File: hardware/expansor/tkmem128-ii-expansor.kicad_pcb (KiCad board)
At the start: 2 copper layers, 78.7 x 45 mm, 3 parts, among them J1 Terminais do conector, J2 Passagem

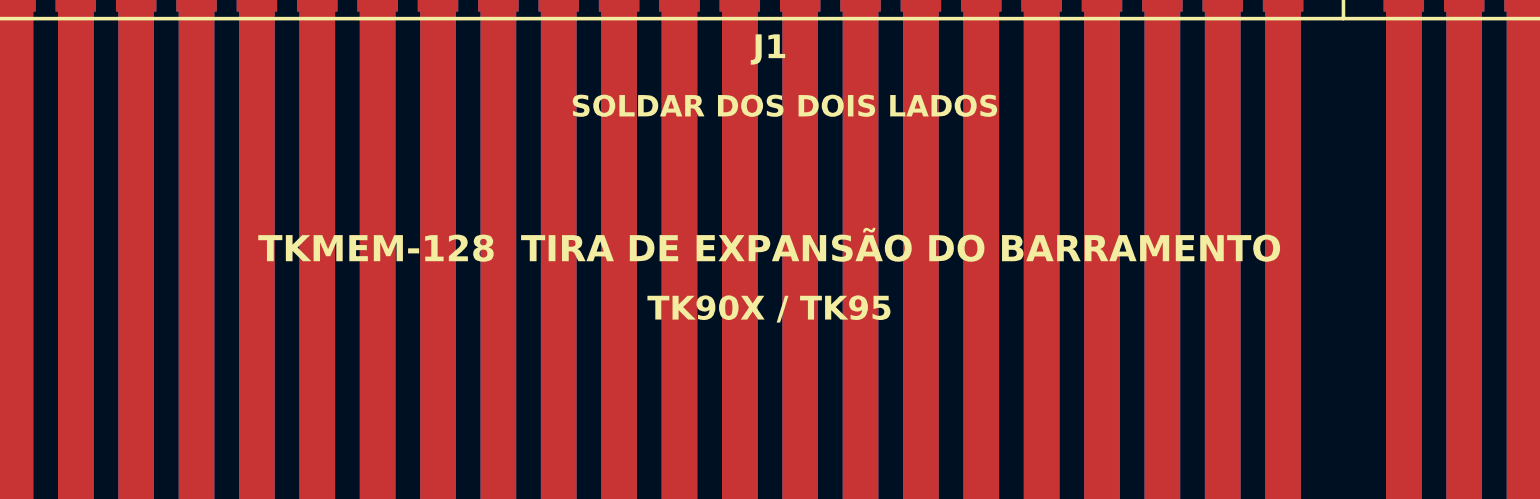
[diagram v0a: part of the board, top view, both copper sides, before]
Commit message: Projeto passa a se chamar TKMEM-128 II
"TKMEM-128 KiCad" dizia so que mudou de software de CAD, quando na verdade a
placa e outra: 4 camadas, trilha do dobro, roteamento e posicionamento refeitos,
JP4 e SJ1/SJ2 fora, auto-desativacao em outro pino, compatibilidade com o ZX
Spectrum recuperada. "II" nomeia a geracao, e manter "TKMEM-128" no nome mantem
a linhagem visivel.

O CUIDADO PRINCIPAL foi nao apagar o credito. "TKMEM-128" aparece no repositorio
nos dois sentidos, e so o primeiro virou "II":

  a NOSSA placa  titulo do README, serigrafia das duas placas, gal/README, duas
                 frases do PREPARAR-O-TK
  a do LUCCAS    a linha da tabela de derivacao, o diagrama de linhagem, "o autor
                 da TKMEM-128 original deixou de fornecer a ROM", e o titulo do
                 artigo dele citado no PREPARAR-O-TK — esses ficaram intactos

Uma substituicao global teria reescrito a atribuicao, que e justamente o que a
CERN-OHL-S existe para proteger.

ARQUIVOS. Os do projeto KiCad seguiram o nome:

  hardware/tkmem128.kicad_{pro,sch,pcb,dru}          -> tkmem128-ii.*
  hardware/expansor/tkmem128-expansor.*             -> tkmem128-ii-expansor.*
  gerbers                                            -> tkmem128-ii-F_Cu.gbr etc.

A BIBLIOTECA NAO. `hardware/lib/tkmem128.pretty` e `tkmem128.kicad_sym` continuam
com o nome antigo de proposito: sao um acervo de footprints do barramento do TK,
nao do projeto, e renomea-las obrigaria a reescrever o prefixo `tkmem128:` em
cada componente das duas placas — superficie de erro sem ganho. Mesmo raciocinio
para `hardware/gal/tkmem128.pld/.jed`, que e o mapa de fusiveis herdado.

Repositorio renomeado para github.com/lrrosa/tkmem128-ii (o GitHub redireciona o
endereco antigo). A URL na serigrafia das duas placas acompanhou.

De quebra: com tres caracteres a mais, o titulo na serigrafia da principal — que
e centralizado — cresceu para os dois lados e encostou em R4. Deslocado 5 mm.

DRC 0/0 na principal, 0 violacoes na t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
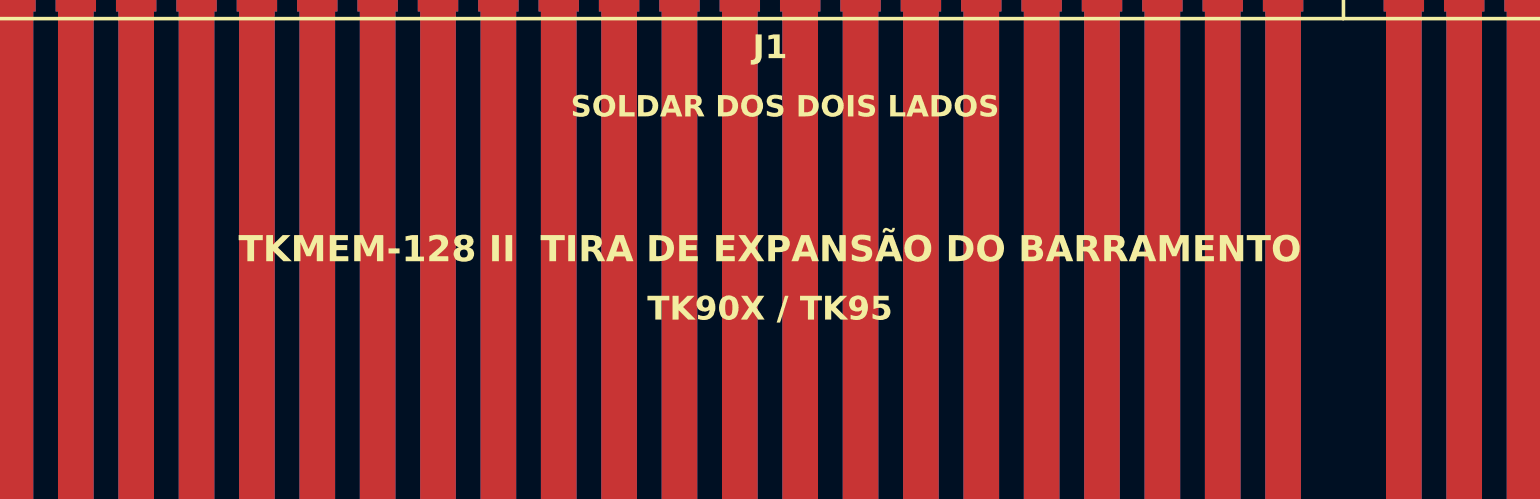
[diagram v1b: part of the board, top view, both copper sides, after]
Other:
- board text added: "CERN-OHL-S v2 | github.com/lrrosa/tkmem128-ii"
- board text added: "TKMEM-128 II TIRA DE EXPANSÃO DO BARRAMENTO"
- board text removed: "CERN-OHL-S v2 | github.com/lrrosa/tkmem128-kicad"
- board text removed: "TKMEM-128 TIRA DE EXPANSÃO DO BARRAMENTO"
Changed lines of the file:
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@@
 		)
 	)
-	(gr_text "TKMEM-128  TIRA DE EXPANSÃO DO BARRAMENTO"
+	(gr_text "TKMEM-128 II  TIRA DE EXPANSÃO DO BARRAMENTO"
 		(at 39.37 15 0)
 		(layer "F.SilkS")
@@
 		)
 	)
-	(gr_text "CERN-OHL-S v2  |  github.com/lrrosa/tkmem128-kicad"
+	(gr_text "CERN-OHL-S v2  |  github.com/lrrosa/tkmem128-ii"
 		(at 39.37 22 0)
 		(layer "B.SilkS")

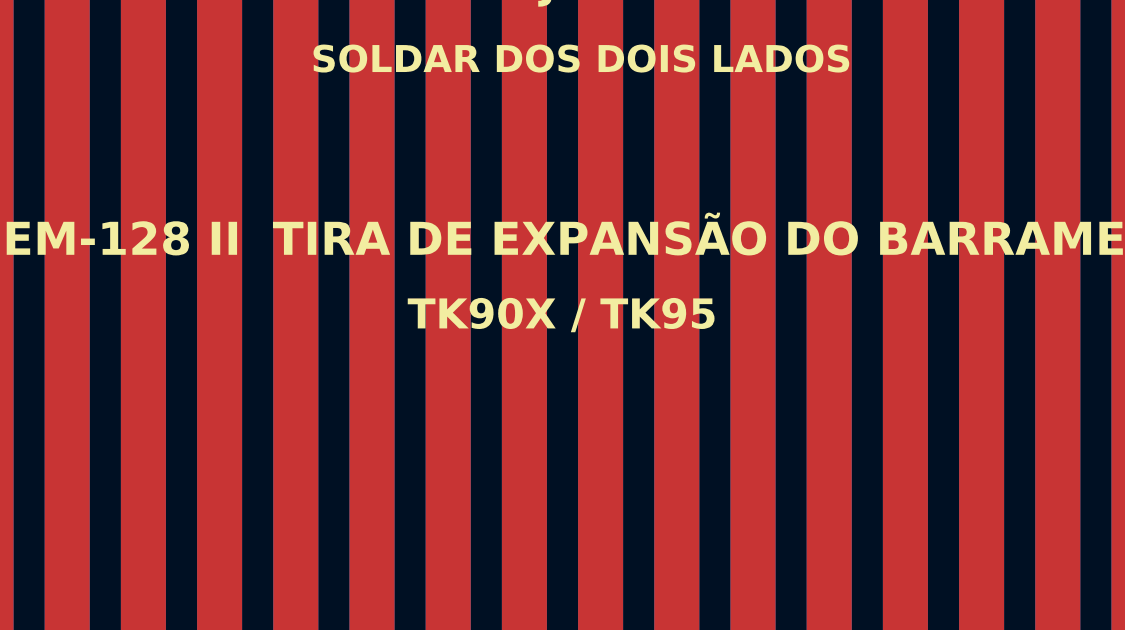
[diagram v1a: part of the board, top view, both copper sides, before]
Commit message: Legenda diz ZX Spectrum 48K e clones — e o pino 17 parou de mentir
O bloco de titulo dos dois esquematicos dizia "para TK90X/TK95". Errado desde
que a placa voltou a servir no ZX Spectrum 48K: o circuito e do Velesoft e
nasceu para o Spectrum, os TKs e que sao os clones. Agora diz "ZX Spectrum 48K
e clones", e o mesmo vale para o titulo em netlist.py/netlist_exp.py e para as
descricoes de simbolo e footprint.

De quebra, a mesma afirmacao errada estava na SERIGRAFIA da tira, em F.SilkS —
essa sai impressa na placa. Virou "ZX SPECTRUM 48K E CLONES".

Os `tags`/`ki_keywords` continuam citando TK90X e TK95 de proposito: ali listar
as duas familias e justamente o que se quer, sao palavras de busca.

O QUE APARECEU AO REGERAR A BIBLIOTECA. O simbolo do conector ainda rotulava
**pino 17 = RAMDIS e pino 29 = NC** — a pinagem de ANTES de mover a
auto-desativacao da RAM para o pino 29 por causa do video componente do
Spectrum. E tinha chegado aos dois esquematicos: o PDF entregue desenhava
exatamente a ligacao que fomos evitar, com o rotulo do pino contradizendo o
fio ligado nele (o global label ja dizia BUS_P17). Quatro rotulos por
esquematico: 16, 17, 18 e 29.

E a terceira vez que uma copia envelhece em silencio aqui — antes foram a ilha
do conector (biblioteca com 1,75 enquanto a placa usava 1,50) e o titulo do
bloco de legenda. Entao virou conferidor: `tools/confere_pinos.py` compara os
rotulos dos dois esquematicos e da biblioteca contra busdef.py, que e a fonte
unica da pinagem. Conferido com teste negativo nos dois formatos.

Detalhe que quase deixou o conferidor inutil: o gerador escreve "ROTULO (nn)"
com espaco, e e assim que fica no .kicad_sym, mas o KiCad troca por underscore
ao salvar um .kicad_sch. A primeira versao do padrao so aceitava underscore,
lia ZERO pino na biblioteca e passava "sem divergencia".

DRC 0/0 na principal, 0 violacoes na tira, ERC 0, os cinco conferidores OK.

Co-Authored-By: Claude Opus 5 <noreply@anthropic.com>
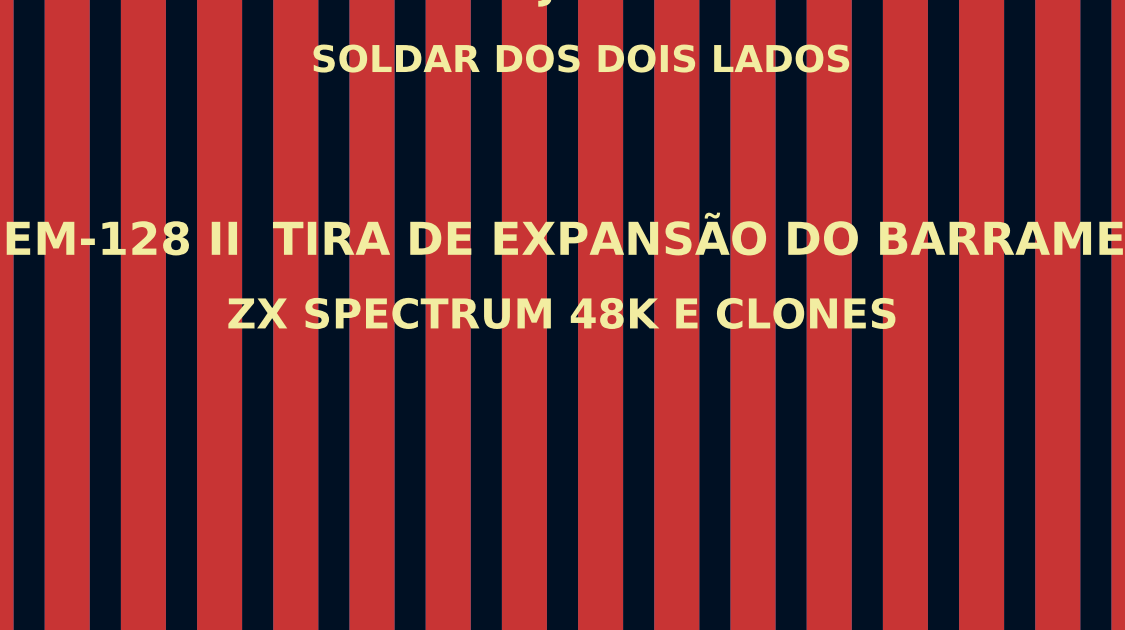
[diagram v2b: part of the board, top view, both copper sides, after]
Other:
- board text added: "ZX SPECTRUM 48K E CLONES"
- board text removed: "TK90X / TK95"
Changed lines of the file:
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@@
 		(layer "F.Cu")
 		(at 39.37 41.19 180)
-		(descr "Dedos de borda 56 vias (28x2) passo 2,54mm para passagem do barramento TK90X/TK95. Requer chanfro 45 graus e ouro ENIG. Coluna 5 = guia (rasgo no contorno da placa).")
+		(descr "Dedos de borda 56 vias (28x2) passo 2,54mm para passagem do barramento do ZX Spectrum 48K e clones. Requer chanfro 45 graus e ouro ENIG. Coluna 5 = guia (rasgo no contorno da placa).")
 		(tags "conector borda edge fingers 56 ZX Spectrum TK90X TK95 passthrough")
 		(property "Reference" "J2"
@@
 		)
 	)
-	(gr_text "TK90X / TK95"
+	(gr_text "ZX SPECTRUM 48K E CLONES"
 		(at 39.37 17.5 0)
 		(layer "F.SilkS")
